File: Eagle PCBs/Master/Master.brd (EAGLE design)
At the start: 87.3 x 40.6 mm, 15 parts

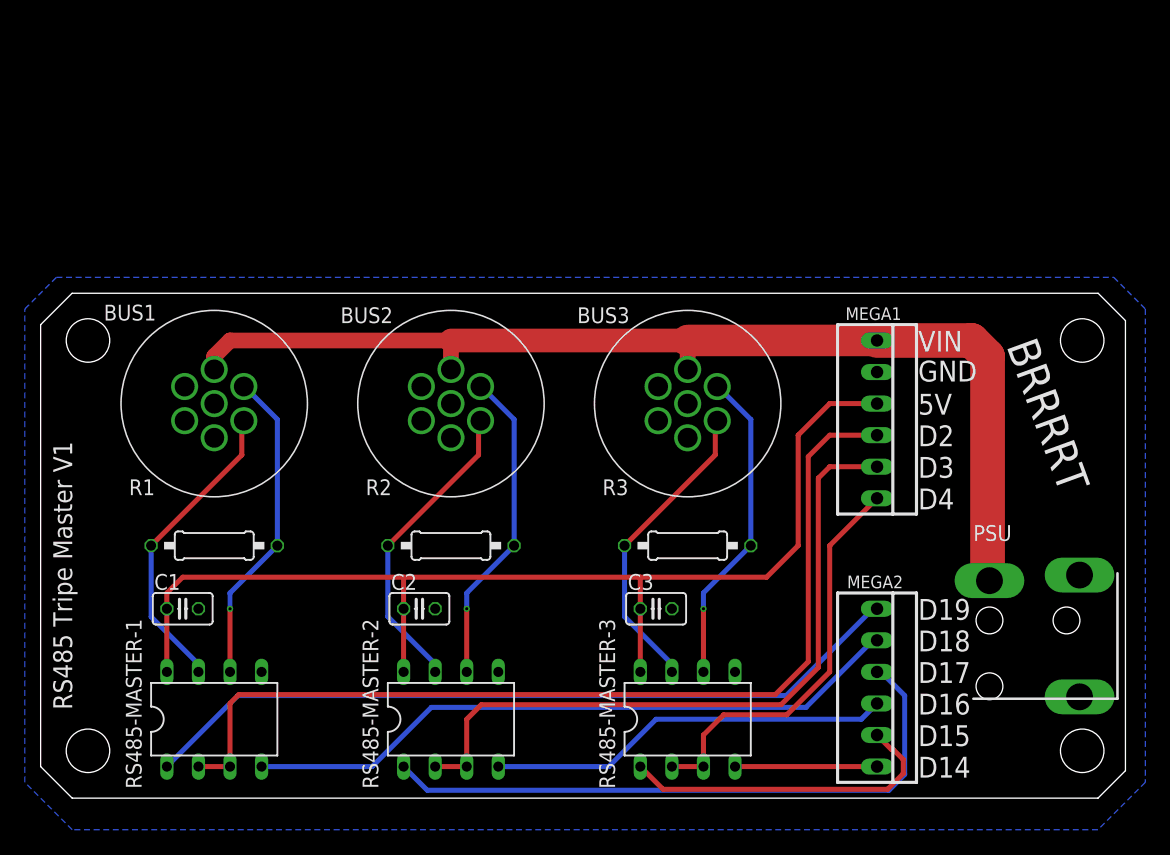
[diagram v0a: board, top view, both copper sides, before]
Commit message: Minor PCB adjustments
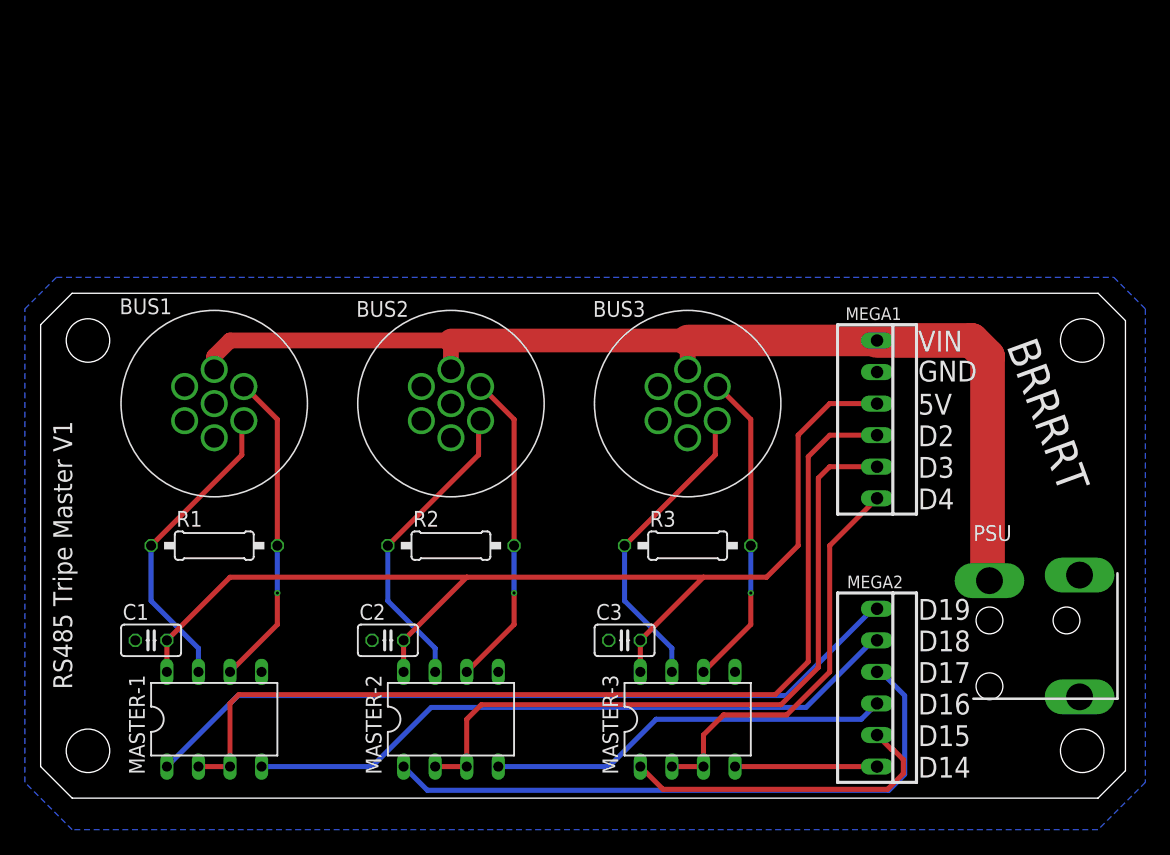
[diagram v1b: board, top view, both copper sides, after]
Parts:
- moved C1 3.59 mm to (8.89, 12.7), turned to 180 degrees
- moved C2 3.59 mm to (27.9, 12.7), turned to 180 degrees
- moved C3 3.59 mm to (47.0, 12.7), turned to 180 degrees
- renumbered RS485-MASTER-1 to MASTER-1, RS485-MASTER-2 to MASTER-2, RS485-MASTER-3 to MASTER-3
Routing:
- net 5VCC: track 90.3 -> 92.2 mm

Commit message: Minor PCB adjustments
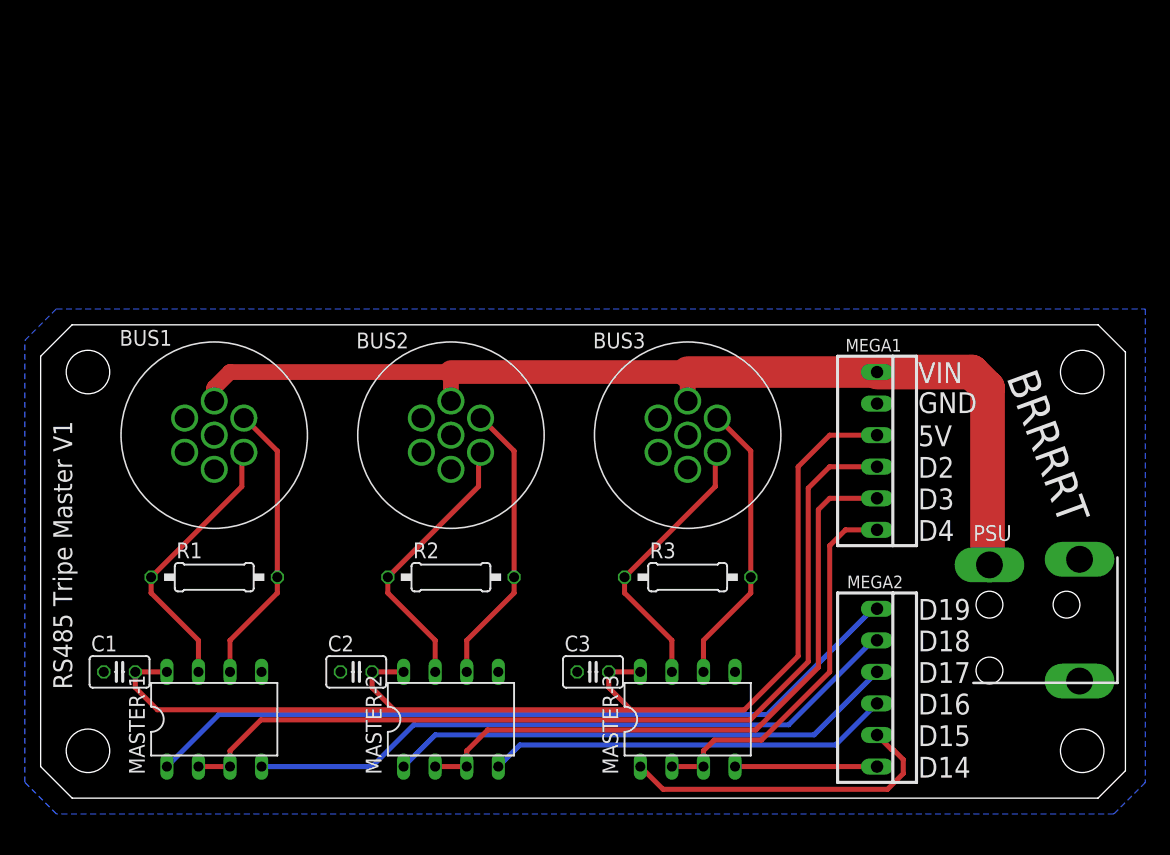
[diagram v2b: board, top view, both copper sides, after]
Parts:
- moved C2 3.59 mm to (25.4, 10.2)
- moved C1 3.59 mm to (6.35, 10.2)
- moved C3 3.59 mm to (44.5, 10.2)
- moved BUS1 2.54 mm to (14.0, 29.2)
- moved BUS2 2.54 mm to (33.0, 29.2)
- moved BUS3 2.54 mm to (52.1, 29.2)
- moved MEGA1 2.54 mm to (67.3, 27.9)
- moved R1 2.54 mm to (14.0, 17.8)
- moved R2 2.54 mm to (33.0, 17.8)
- moved R3 2.54 mm to (52.1, 17.8)
- moved PSU 1.27 mm to (80.1, 14.4)
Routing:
- net MEGA_D17: track 51.0 -> 41.3 mm
- net MEGA_D2: track 78.3 -> 73.5 mm
- net MEGA_D3: track 56.7 -> 52.7 mm
- net VCC: track 87.1 -> 83.3 mm
- net 5VCC: track 92.2 -> 95.0 mm
- net RS485_3_A: track 25.7 -> 23.2 mm, vias 1 -> 0
- net RS485_2_A: track 25.7 -> 23.2 mm, vias 1 -> 0
- net RS485_1_B: track 24.9 -> 22.3 mm
- net RS485_1_A: track 25.7 -> 23.2 mm, vias 1 -> 0
- net RS485_3_B: track 24.9 -> 22.3 mm
- net RS485_2_B: track 24.9 -> 22.3 mm
- net MEGA_D4: track 32.9 -> 31.1 mm
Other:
- board size 87.3 x 40.6 mm -> 87.3 x 38.1 mm

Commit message: Added a 5v bus to all PCBs
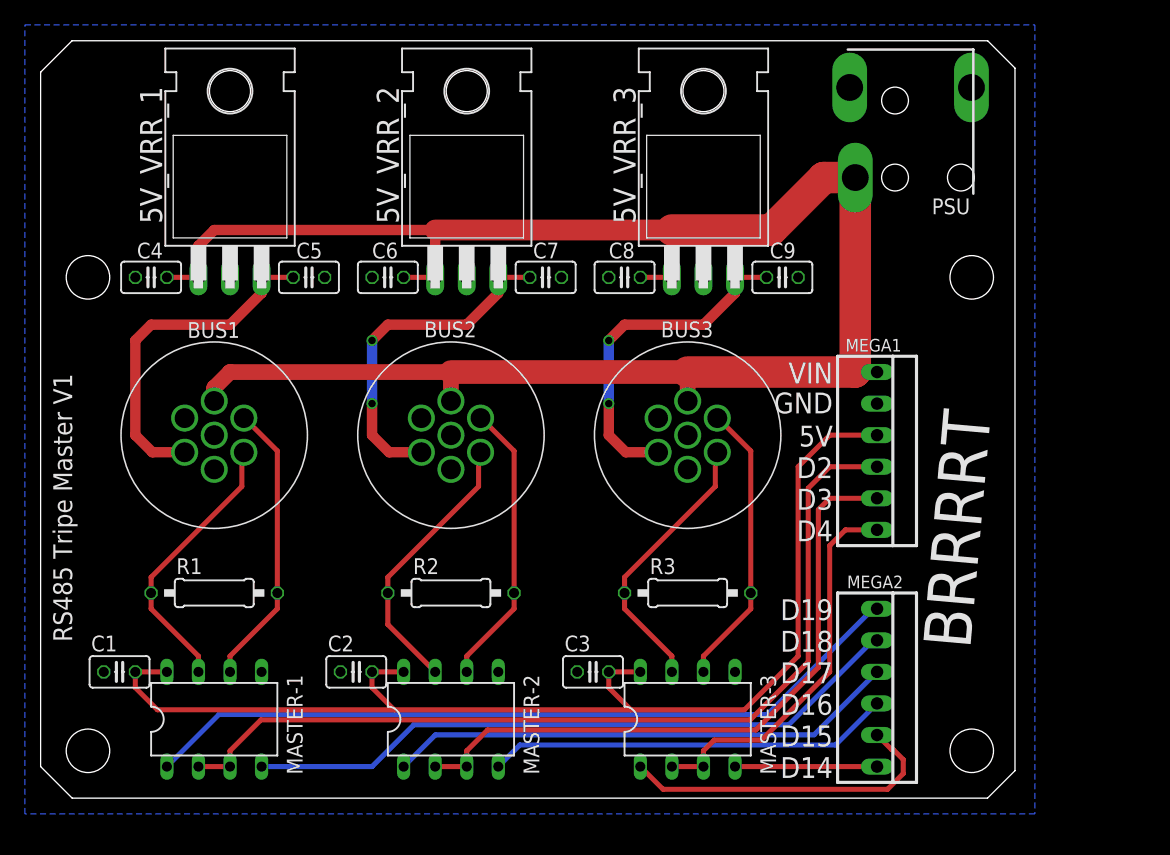
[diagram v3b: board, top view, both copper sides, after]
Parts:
- added 5V_VRR_1, 5V_VRR_2, 5V_VRR_3: L7805CV, linear:TO220H
- added C4, C6, C8: 0.33uF, rcl:C025-025X050
- added C5, C7, C9: 0.1uF, rcl:C025-025X050
- moved PSU 40.7 mm to (70.0, 53.7), turned to 180 degrees
- moved R1 1.27 mm to (14.0, 16.5)
- moved R2 1.27 mm to (33.0, 16.5)
- moved R3 1.27 mm to (52.1, 16.5)
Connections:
- new net 5VCC_BUS1: 5V_VRR_1.3, BUS1.5, C5.1
- new net 5VCC_BUS2: 5V_VRR_2.3, BUS2.5, C7.1
- new net 5VCC_BUS3: 5V_VRR_3.3, BUS3.5, C9.1
- net GND: now also 5V_VRR_1.2, 5V_VRR_2.2, 5V_VRR_3.2, C4.2, C5.2, C6.2, C7.2, C8.2, C9.2
- net VCC: now also 5V_VRR_1.1, 5V_VRR_2.1, 5V_VRR_3.1, C4.1, C6.1, C8.1
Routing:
- net VCC: track 83.3 -> 148.2 mm
- net 5VCC_BUS3: track 0.00 -> 27.7 mm, vias 0 -> 2
- net 5VCC_BUS2: track 0.00 -> 27.7 mm, vias 0 -> 2
- net 5VCC_BUS1: track 0.00 -> 27.7 mm
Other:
- board size 87.3 x 38.1 mm -> 78.4 x 61 mm
